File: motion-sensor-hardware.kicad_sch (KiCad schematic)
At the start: 6 parts, among them Q1 BSS138, U1 ESP32-DevKitC, U2 LD2410C

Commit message: Generated artwork
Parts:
- added H1, H2, H3, H4: MountingHole, MountingHole:MountingHole_3.2mm_M3, symbol Mechanical:MountingHole

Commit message: WIP
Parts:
- added J1: USB_C_Receptacle_USB2.0_16P, symbol Connector:USB_C_Receptacle_USB2.0_16P
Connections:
- new net: J1.A1 (GND), J1.A12 (GND), J1.B1 (GND), J1.B12 (GND)
- new net: J1.A4 (VBUS), J1.A9 (VBUS), J1.B4 (VBUS), J1.B9 (VBUS)
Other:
- added sheet Voltage Regulator (regulator.kicad_sch)
- moved on the sheet: H1, H2, H3, H4
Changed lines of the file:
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@@
 	(symbol
 		(lib_id "Mechanical:MountingHole")
-		(at 210.82 29.21 0)
+		(at 273.05 24.13 0)
 		(unit 1)
 		(exclude_from_sim no)
@@
 		(fields_autoplaced yes)
 		(property "Reference" "H1"
-			(at 213.36 29.2099 0)
+			(at 275.59 24.1299 0)
 			(effects
 				(font
@@
 		)
 		(property "Value" "MountingHole"
-			(at 213.36 30.4799 0)
+			(at 275.59 25.3999 0)
 			(effects
 				(font
@@
 		)
 		(property "Footprint" "MountingHole:MountingHole_3.2mm_M3"
-			(at 210.82 29.21 0)
+			(at 273.05 24.13 0)
 			(effects
 				(font
@@
 		)
 		(property "Datasheet" "~"
-			(at 210.82 29.21 0)
+			(at 273.05 24.13 0)
 			(effects
 				(font
@@
 		)
 		(property "Description" "Mounting Hole without connection"
-			(at 210.82 29.21 0)
+			(at 273.05 24.13 0)
 			(effects
 				(font
@@
 				(path "/d999e802-7382-49ed-b28b-80393e8497d9"
 					(reference "H1")
+					(unit 1)
+				)
+			)
+		)
+	)
+	(symbol
+		(lib_id "Connector:USB_C_Receptacle_USB2.0_16P")
+		(at 201.93 53.34 0)
+		(unit 1)
+		(exclude_from_sim no)
+		(in_bom yes)
+		(on_board yes)
+		(dnp no)
+		(fields_autoplaced yes)
+		(property "Reference" "J1"
+			(at 201.93 30.48 0)
+			(effects
+				(font
+					(size 1.27 1.27)
+				)
+			)
+		)
+		(property "Value" "USB_C_Receptacle_USB2.0_16P"
+			(at 201.93 33.02 0)
+			(effects
+				(font
+					(size 1.27 1.27)
+				)
+			)
+		)
+		(property "Footprint" ""
+			(at 205.74 53.34 0)
+			(effects
+				(font
+					(size 1.27 1.27)
+				)
+				(hide yes)
+			)
+		)
+		(property "Datasheet" "https://www.usb.org/sites/default/files/documents/usb_type-c.zip"
+			(at 205.74 53.34 0)
+			(effects
+				(font
+					(size 1.27 1.27)
+				)
+				(hide yes)
+			)
+		)
+		(property "Description" "USB 2.0-only 16P Type-C Receptacle connector"
+			(at 201.93 53.34 0)
+			(effects
+				(font
+					(size 1.27 1.27)
+				)
+				(hide yes)
+			)
+		)
+		(pin "A6"
+		)
+		(pin "S1"
+		)
+		(pin "B6"
+		)
+		(pin "A12"
+		)
+		(pin "B12"
+		)
+		(pin "A7"
+		)
+		(pin "A1"
+		)
+		(pin "B4"
+		)
+		(pin "B7"
+		)
+		(pin "B9"
+		)
+		(pin "A8"
+		)
+		(pin "A5"
+		)
+		(pin "B1"
+		)
+		(pin "B5"
+		)
+		(pin "A4"
+		)
+		(pin "A9"
+		)
+		(pin "B8"
+		)
+		(instances
+			(project ""
+				(path "/d999e802-7382-49ed-b28b-80393e8497d9"
+					(reference "J1")
 					(unit 1)
 				)
@@
 	(symbol
 		(lib_id "Mechanical:MountingHole")
-		(at 210.82 35.56 0)
+		(at 273.05 30.48 0)
 		(unit 1)
 		(exclude_from_sim no)
@@
 		(fields_autoplaced yes)
 		(property "Reference" "H2"
-			(at 213.36 35.5599 0)
+			(at 275.59 30.4799 0)
 			(effects
 				(font
@@
 		)
 		(property "Value" "MountingHole"
-			(at 213.36 36.8299 0)
+			(at 275.59 31.7499 0)
 			(effects
 				(font
@@
 		)
 		(property "Footprint" "MountingHole:MountingHole_3.2mm_M3"
-			(at 210.82 35.56 0)
+			(at 273.05 30.48 0)
 			(effects
 				(font
@@
 		)
 		(property "Datasheet" "~"
-			(at 210.82 35.56 0)
+			(at 273.05 30.48 0)
 			(effects
 				(font
@@
 		)
 		(property "Description" "Mounting Hole without connection"
-			(at 210.82 35.56 0)
+			(at 273.05 30.48 0)
 			(effects
 				(font
@@
 	(symbol
 		(lib_id "Mechanical:MountingHole")
-		(at 210.82 48.26 0)
+		(at 273.05 43.18 0)
 		(unit 1)
 		(exclude_from_sim no)
@@
 		(fields_autoplaced yes)
 		(property "Reference" "H4"
-			(at 213.36 48.2599 0)
+			(at 275.59 43.1799 0)
 			(effects
 				(font
@@
 		)
 		(property "Value" "MountingHole"
-			(at 213.36 49.5299 0)
+			(at 275.59 44.4499 0)
 			(effects
 				(font
@@
 		)
 		(property "Footprint" "MountingHole:MountingHole_3.2mm_M3"
-			(at 210.82 48.26 0)
+			(at 273.05 43.18 0)
 			(effects
 				(font
@@
 		)
 		(property "Datasheet" "~"
-			(at 210.82 48.26 0)
+			(at 273.05 43.18 0)
 			(effects
 				(font
@@
 		)
 		(property "Description" "Mounting Hole without connection"
-			(at 210.82 48.26 0)
+			(at 273.05 43.18 0)
 			(effects
 				(font
@@
 	(symbol
 		(lib_id "Mechanical:MountingHole")
-		(at 210.82 41.91 0)
+		(at 273.05 36.83 0)
 		(unit 1)
 		(exclude_from_sim no)
@@
 		(fields_autoplaced yes)
 		(property "Reference" "H3"
-			(at 213.36 41.9099 0)
+			(at 275.59 36.8299 0)
 			(effects
 				(font
@@
 		)
 		(property "Value" "MountingHole"
-			(at 213.36 43.1799 0)
+			(at 275.59 38.0999 0)
 			(effects
 				(font
@@
 		)
 		(property "Footprint" "MountingHole:MountingHole_3.2mm_M3"
-			(at 210.82 41.91 0)
+			(at 273.05 36.83 0)
 			(effects
 				(font
@@
 		)
 		(property "Datasheet" "~"
-			(at 210.82 41.91 0)
+			(at 273.05 36.83 0)
 			(effects
 				(font
@@
 		)
 		(property "Description" "Mounting Hole without connection"
-			(at 210.82 41.91 0)
+			(at 273.05 36.83 0)
 			(effects
 				(font
@@
 				)
 			)
+		)
+	)
+	(sheet
+		(at 140.335 27.94)
+		(size 12.7 5.715)
+		(exclude_from_sim no)
+		(in_bom yes)
+		(on_board yes)
+		(dnp no)
+		(fields_autoplaced yes)
+		(stroke
+			(width 0.1524)
+			(type solid)
+		)
+		(fill
+			(color 0 0 0 0.0000)
+		)
+		(property "Sheetname" "Voltage Regulator"
+			(at 140.335 27.2284 0)
+			(effects
+				(font
+					(size 1.27 1.27)
+				)
+				(justify left bottom)
+			)
+		)
+		(property "Sheetfile" "regulator.kicad_sch"
+			(at 140.335 34.2396 0)
+			(effects
+				(font
+					(size 1.27 1.27)
+				)
+				(justify left top)
+			)
+		)
+		(pin "VIN" input
+			(at 140.335 30.48 180)
+			(effects
+				(font
+					(size 1.27 1.27)
+				)
+				(justify left)
+			)
+		)
+		(pin "V_{OUT}" input
+			(at 153.035 30.48 0)
+			(effects
+				(font
+					(size 1.27 1.27)
+				)
+				(justify right)
+			)
+		)
+		(instances
+			(project "motion-sensor-hardware"
+				(path "/d999e802-7382-49ed-b28b-80393e8497d9"
+					(page "2")
+				)
+			)

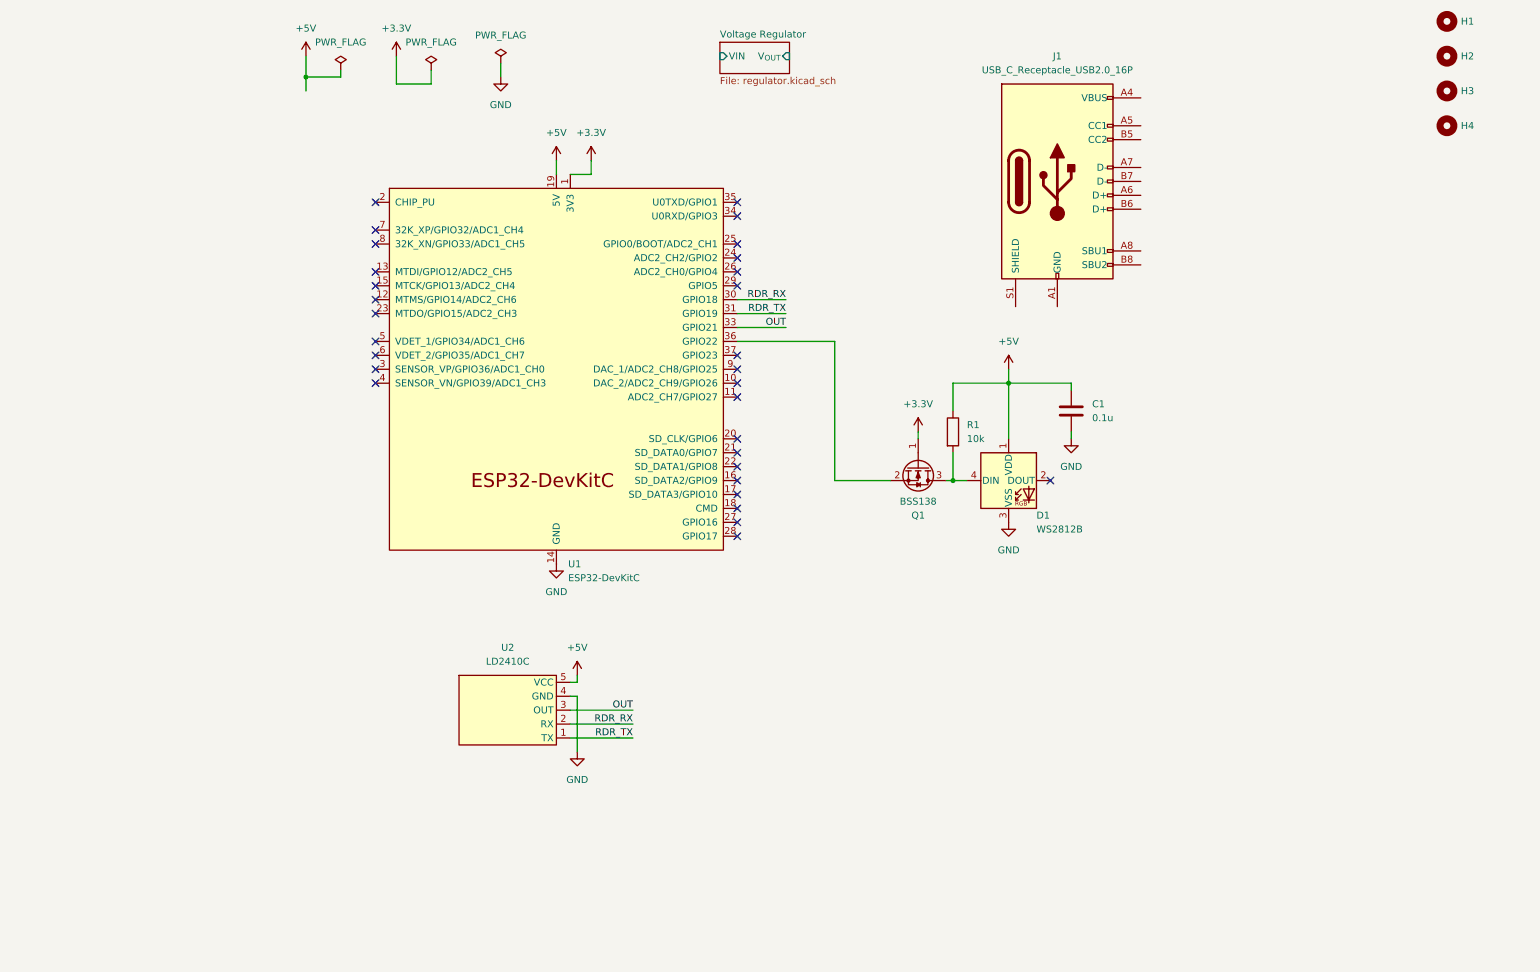
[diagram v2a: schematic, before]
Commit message: Switching converter for 12 V -> 5V. LDO for 5->3
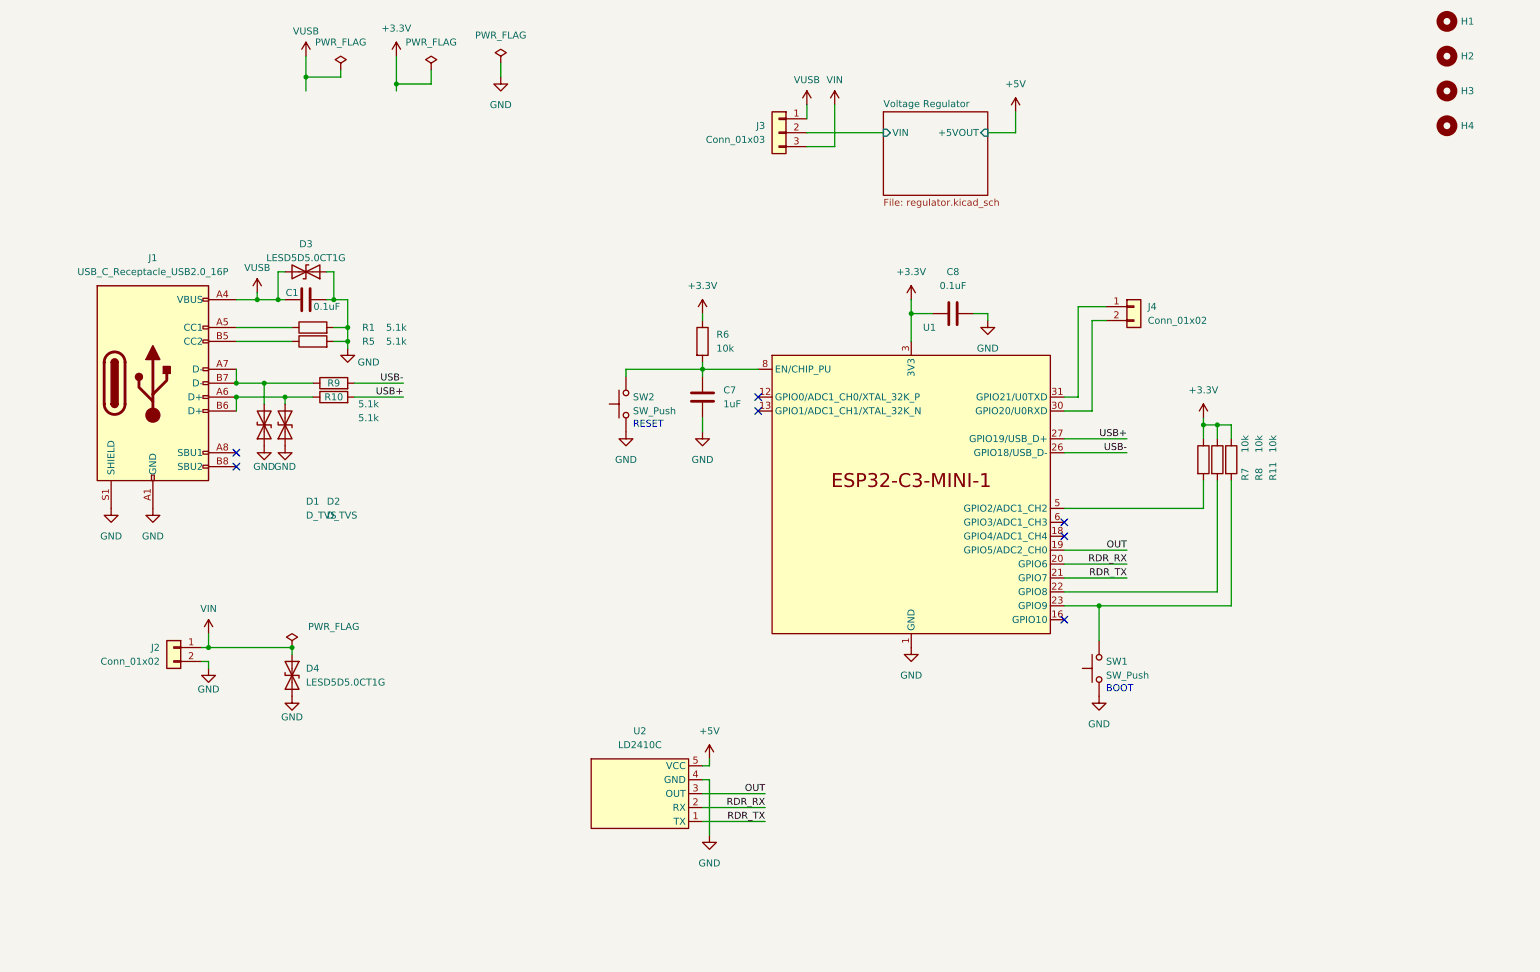
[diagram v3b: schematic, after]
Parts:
- removed D1: WS2812B, LED_SMD:LED_WS2812B_PLCC4_5.0x5.0mm_P3.2mm, symbol LED:WS2812B
- removed Q1: BSS138, Package_TO_SOT_SMD:SOT-23, symbol Transistor_FET:BSS138
- removed U1: ESP32-DevKitC, ESP32-DevkitC-32:ESP32-DevKitC, symbol motion-sensor-syms:ESP32-DevKitC
- added C7: 1uF, symbol Device:C
- added C8: 0.1uF, symbol Device:C
- added D1, D2: D_TVS, symbol Device:D_TVS
- added D3, D4: LESD5D5.0CT1G, symbol Device:D_TVS
- added J2, J4: Conn_01x02, symbol Connector_Generic:Conn_01x02
- added J3: Conn_01x03, symbol Connector_Generic:Conn_01x03
- added R10, R5, R9: 5.1k, symbol Device:R
- added R11, R6, R7, R8: 10k, symbol Device:R
- added SW1, SW2: SW_Push, symbol Switch:SW_Push
- added U1: ~, symbol motion-sensor-syms:ESP32-C3-MINI-1
- C1: value 0.1u -> 0.1uF; footprint Capacitor_SMD:C_0805_2012Metric_Pad1.18x1.45mm_HandSolder -> (none)
- R1: value 10k -> 5.1k; footprint Resistor_SMD:R_0805_2012Metric_Pad1.20x1.40mm_HandSolder -> (none)
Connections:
- net +3.3V: now also C8.1, R11.1, R6.1, R7.1, R8.1, U1.3 (3V3)
- net +5V: no longer C1.1, R1.1
- net GND: now also J1.A1 (GND), J1.A12 (GND), J1.B1 (GND), J1.B12 (GND), J1.S1 (SHIELD), R1.2, C7.2, C8.2, D1.1 (A1), D2.1 (A1), D3.1 (A1), D4.2 (A2), J2.2 (Pin_2), R5.2, SW1.1, SW2.1, U1.1 (GND), U1.11 (GND), U1.14 (GND), U1.2 (GND), U1.36 (GND), U1.37 (GND), U1.38 (GND), U1.39 (GND), U1.40 (GND), U1.41 (GND), U1.42 (GND), U1.43 (GND), U1.44 (GND), U1.45 (GND), U1.46 (GND), U1.47 (GND), U1.48 (GND), U1.49 (GND), U1.50 (GND), U1.51 (GND), U1.52 (GND), U1.53 (GND)
- net OUT: now also U1.19 (GPIO5/ADC2_CH0)
- net RDR_RX: now also U1.20 (GPIO6)
- net RDR_TX: now also U1.21 (GPIO7)
- net Voltage Regulator/VIN: now also J3.2 (Pin_2)
- net VUSB: now reaches J1.A4 (VBUS), J1.A9 (VBUS), J1.B4 (VBUS), J1.B9 (VBUS)
- net VUSB: now also C1.1, D3.2 (A2), J3.1 (Pin_1)
- net at J1.A5 (CC1): now also R1.1
- net at J1.A6 (D+): now also J1.B6 (D+), D2.2 (A2), R10.1
- net at J1.A7 (D-): now also J1.B7 (D-), D1.2 (A2), R9.1
- net at J1.B5 (CC2): now also R5.1
- new net: R8.2, U1.22 (GPIO8)
- new net: C7.1, R6.2, SW2.2, U1.8 (EN/CHIP_PU)
- new net: R11.2, SW1.2, U1.23 (GPIO9)
- new net: J4.2 (Pin_2), U1.30 (GPIO20/U0RXD)
- new net: J4.1 (Pin_1), U1.31 (GPIO21/U0TXD)
- new net: R7.2, U1.5 (GPIO2/ADC1_CH2)
- new net USB+: R10.2, U1.27 (GPIO19/USB_D+)
- new net USB-: R9.2, U1.26 (GPIO18/USB_D-)
- new net VIN: D4.1 (A1), J2.1 (Pin_1), J3.3 (Pin_3)
- no-connect marks 30 -> 7
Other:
- sheet Voltage Regulator ports: added +5VOUT; removed V_{OUT}
- note added: "BOOT"
- note added: "RESET"
- moved on the sheet: J1, U2

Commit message: Added car charger circuits
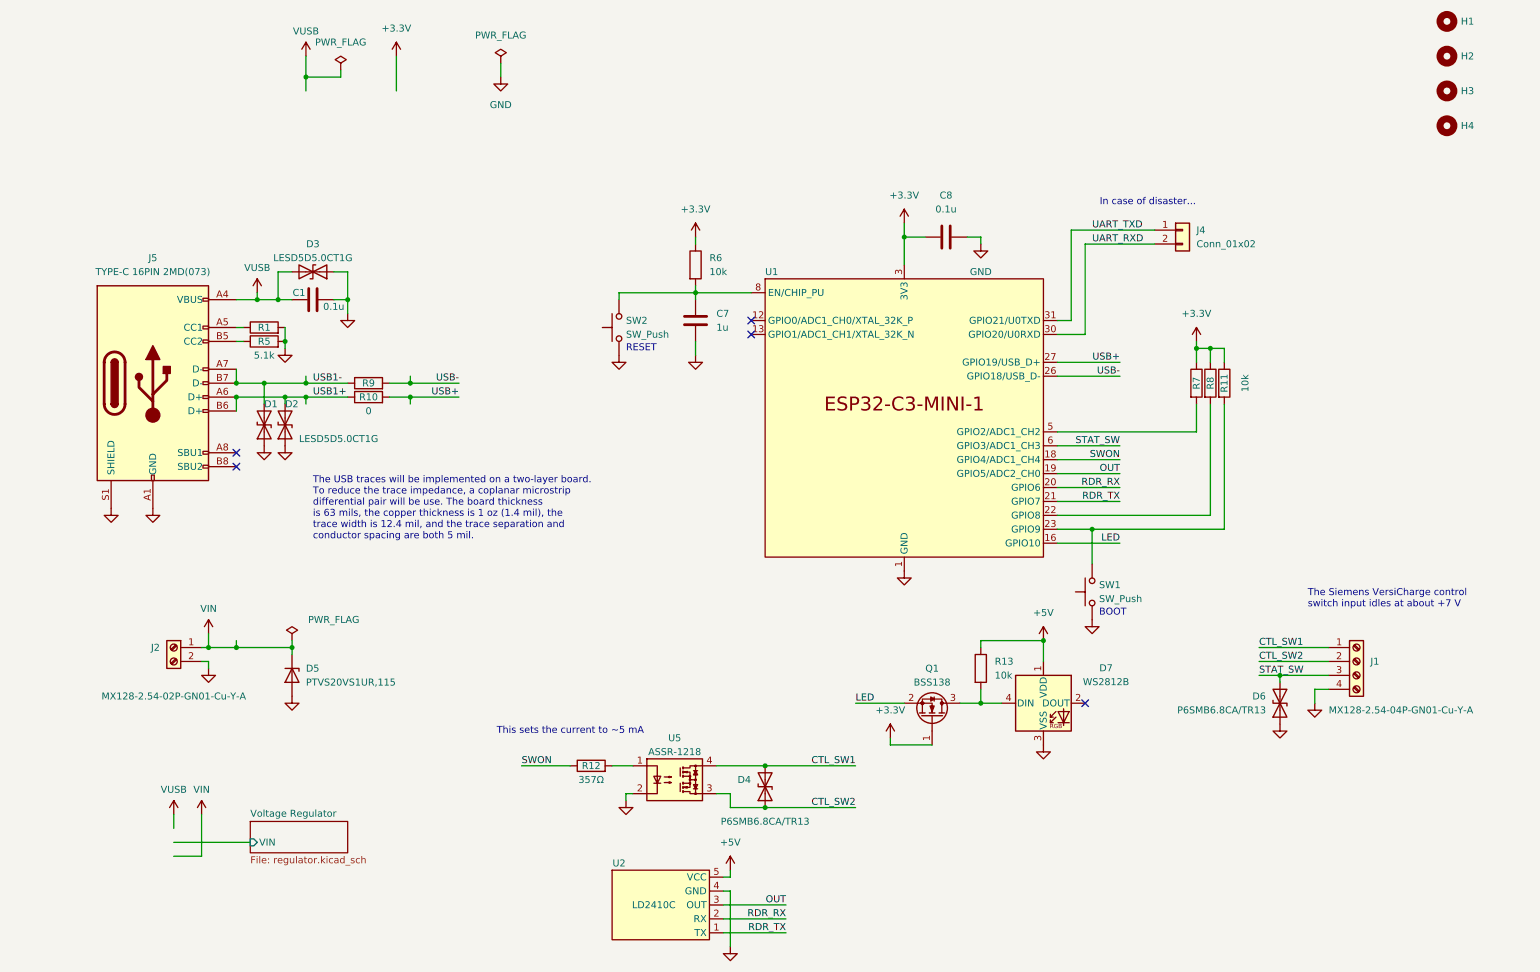
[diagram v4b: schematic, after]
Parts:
- removed J1: USB_C_Receptacle_USB2.0_16P, symbol Connector:USB_C_Receptacle_USB2.0_16P
- removed J3: Conn_01x03, symbol Connector_Generic:Conn_01x03
- added D5: PTVS20VS1UR,115, Diode_SMD:Nexperia_DSN1608-2_1.6x0.8mm, symbol Diode:PTVS26VZ1USK
- added D6: P6SMB6.8CA/TR13, Diode_SMD:D_SMB_Handsoldering, symbol Device:D_TVS
- added D7: WS2812B, LED_SMD:LED_WS2812B_PLCC4_5.0x5.0mm_P3.2mm, symbol LED:WS2812B
- added J1: MX128-2.54-04P-GN01-Cu-Y-A, symbol Connector:Screw_Terminal_01x04
- added J5: TYPE-C 16PIN 2MD(073), Connector_USB:USB_C_Receptacle_GCT_USB4105-xx-A_16P_TopMnt_Horizontal, symbol Connector:USB_C_Receptacle_USB2.0_16P
- added Q1: BSS138, Package_TO_SOT_SMD:SOT-23, symbol Transistor_FET:BSS138
- added R12: 357Ω, Resistor_SMD:R_0805_2012Metric_Pad1.20x1.40mm_HandSolder, symbol Device:R
- added R13: 10k, Capacitor_SMD:C_0805_2012Metric, symbol Device:R
- added U5: ASSR-1218, Package_SO:SO-4_4.4x4.3mm_P2.54mm, symbol Relay_SolidState:ASSR-1218
- C1, C8: value 0.1uF -> 0.1u; footprint (none) -> Capacitor_SMD:C_0805_2012Metric; JLCPCB (none) -> C106837
- C7: value 1uF -> 1u; footprint (none) -> Capacitor_SMD:C_0805_2012Metric; JLCPCB (none) -> C2999517
- D1, D2: value D_TVS -> LESD5D5.0CT1G; footprint (none) -> Diode_SMD:D_SOD-523; JLCPCB (none) -> C383211
- D3: footprint (none) -> Diode_SMD:D_SOD-523; JLCPCB (none) -> C383211
- D4: value LESD5D5.0CT1G -> P6SMB6.8CA/TR13; footprint (none) -> Diode_SMD:D_SMB_Handsoldering; JLCPCB (none) -> C78395
- J2: value Conn_01x02 -> MX128-2.54-02P-GN01-Cu-Y-A; footprint (none) -> My_Connectors:MX300-5.0-02P; symbol Connector_Generic:Conn_01x02 -> Connector:Screw_Terminal_01x02; JLCPCB (none) -> C5188442
- J4: footprint (none) -> Connector_PinHeader_2.54mm:PinHeader_1x02_P2.54mm_Vertical; JLPCB (none) -> C492401
- R1, R5: footprint (none) -> Capacitor_SMD:C_0805_2012Metric; JLCPCB (none) -> C27834
- R10, R9: value 5.1k -> 0; footprint (none) -> Capacitor_SMD:C_0805_2012Metric; JLCPCB (none) -> C17477
- R11, R6, R7, R8: footprint (none) -> Capacitor_SMD:C_0805_2012Metric; JLCPCB (none) -> C17414
- SW1, SW2: footprint (none) -> Button_Switch_SMD:SW_Push_1P1T_NO_CK_KMR2; JLCPCB (none) -> C221678
- U1: value ~ -> ESP32-C3-MINI-1-N4; footprint (none) -> RF_Module:ESP32-C6-MINI-1; JLCPCB (none) -> C2838502
- U2: JLCPCB (none) -> C19723500
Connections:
- net +3.3V: now also Q1.1 (G)
- net +5V: now also D7.1 (VDD), R13.1
- net GND: now also D5.2 (A), D6.1 (A1), D7.3 (VSS), J1.4 (Pin_4), J5.A1 (GND), J5.A12 (GND), J5.B1 (GND), J5.B12 (GND), J5.S1 (SHIELD), U5.2; no longer D4.2 (A2)
- net VIN: now also D5.1 (K); no longer D4.1 (A1)
- net VUSB: now also J5.A4 (VBUS), J5.A9 (VBUS), J5.B4 (VBUS), J5.B9 (VBUS)
- net USB1-: now reaches D1.2 (A2), R9.1
- net USB1-: now also J5.A7 (D-), J5.B7 (D-)
- net at R1.1: now also J5.A5 (CC1)
- net USB1+: now reaches D2.2 (A2), R10.1
- net USB1+: now also J5.A6 (D+), J5.B6 (D+)
- net at R5.1: now also J5.B5 (CC2)
- net LED: now reaches U1.16 (GPIO10)
- net LED: now also Q1.2 (S)
- net SWON: now reaches U1.18 (GPIO4/ADC1_CH4)
- net SWON: now also R12.1
- net UART_RXD: now reaches J4.2 (Pin_2), U1.30 (GPIO20/U0RXD)
- net UART_TXD: now reaches J4.1 (Pin_1), U1.31 (GPIO21/U0TXD)
- net STAT_SW: now reaches U1.6 (GPIO3/ADC1_CH3)
- net STAT_SW: now also D6.2 (A2), J1.3 (Pin_3)
- new net: D7.4 (DIN), Q1.3 (D), R13.2
- new net: R12.2, U5.1
- new net CTL_SW1: D4.2 (A2), J1.1 (Pin_1), U5.4
- new net CTL_SW2: D4.1 (A1), J1.2 (Pin_2), U5.3
- no-connect marks 7 -> 5
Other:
- sheet Voltage Regulator ports: added none; removed +5VOUT
- note added: "In case of disaster..."
- note added: "The Siemens VersiCharge control switch input idles at about +7 V"
- note added: "The USB traces will be implemented on a two-layer board. To reduce the trace impedance, a coplanar microstrip differential pair will be use. The board thickness is 63 mils, the copper thickness is 1 oz (1.4 mil), the trace width is 12.4 mil, and the trace separation and conductor spacing are both 5 mil."
- note added: "This sets the current to ~5 mA"
- moved on the sheet: C1, D3, J4, R1, R10, R5, R6, R9, SW2, U1, U2
